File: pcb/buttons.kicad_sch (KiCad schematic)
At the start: 9 parts, among them SW2 SW_DPDT_x2, SW3 SW_DPDT_x2, SW4 RotaryEncoder, SW5 SW_DPDT_x2, SW6 SW_DPDT_x2

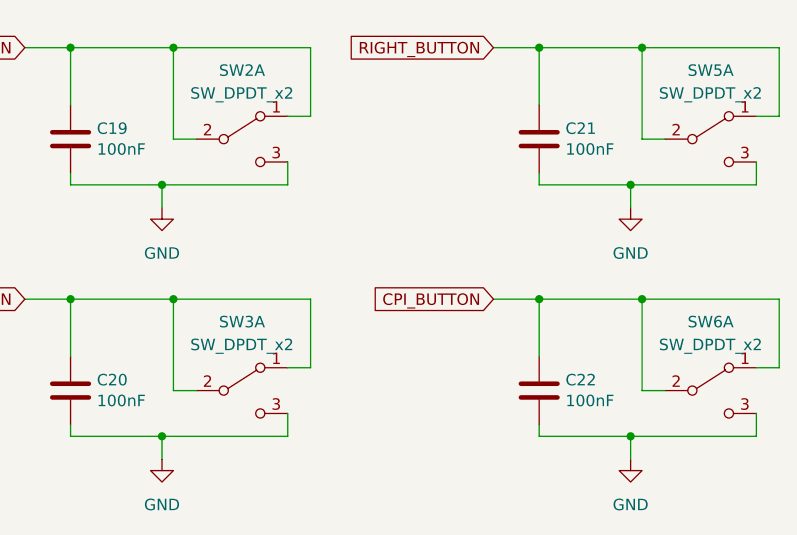
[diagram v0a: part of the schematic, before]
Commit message: cleaned up symbols in schematics a bit
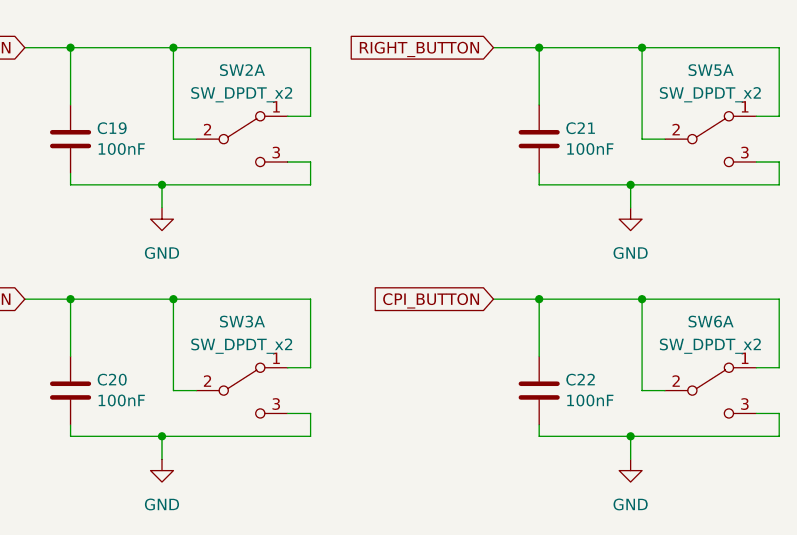
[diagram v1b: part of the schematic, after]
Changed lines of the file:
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@@
     (stroke (width 0) (type default) (color 0 0 0 0))
   )
-  (wire (pts (xy 124.46 96.52) (xy 124.46 93.98))
+  (wire (pts (xy 127 96.52) (xy 127 93.98))
     (stroke (width 0) (type default) (color 0 0 0 0))
   )
@@
     (stroke (width 0) (type default) (color 0 0 0 0))
   )
-  (wire (pts (xy 124.46 124.46) (xy 124.46 121.92))
+  (wire (pts (xy 127 124.46) (xy 127 121.92))
     (stroke (width 0) (type default) (color 0 0 0 0))
   )
   (wire (pts (xy 127 109.22) (xy 127 116.84))
+    (stroke (width 0) (type default) (color 0 0 0 0))
+  )
+  (wire (pts (xy 127 93.98) (xy 124.46 93.98))
     (stroke (width 0) (type default) (color 0 0 0 0))
   )
@@
     (stroke (width 0) (type default) (color 0 0 0 0))
   )
+  (wire (pts (xy 127 121.92) (xy 124.46 121.92))
+    (stroke (width 0) (type default) (color 0 0 0 0))
+  )
   (wire (pts (xy 166.37 119.38) (xy 163.83 119.38))
     (stroke (width 0) (type default) (color 0 0 0 0))
@@
     (stroke (width 0) (type default) (color 0 0 0 0))
   )
-  (wire (pts (xy 176.53 124.46) (xy 176.53 121.92))
+  (wire (pts (xy 179.07 124.46) (xy 179.07 121.92))
     (stroke (width 0) (type default) (color 0 0 0 0))
   )
@@
     (stroke (width 0) (type default) (color 0 0 0 0))
   )
-  (wire (pts (xy 110.49 124.46) (xy 124.46 124.46))
+  (wire (pts (xy 110.49 124.46) (xy 127 124.46))
     (stroke (width 0) (type default) (color 0 0 0 0))
   )
-  (wire (pts (xy 162.56 124.46) (xy 176.53 124.46))
+  (wire (pts (xy 162.56 124.46) (xy 179.07 124.46))
     (stroke (width 0) (type default) (color 0 0 0 0))
   )
-  (wire (pts (xy 110.49 96.52) (xy 124.46 96.52))
+  (wire (pts (xy 110.49 96.52) (xy 127 96.52))
     (stroke (width 0) (type default) (color 0 0 0 0))
   )
@@
   )
   (wire (pts (xy 111.76 109.22) (xy 100.33 109.22))
+    (stroke (width 0) (type default) (color 0 0 0 0))
+  )
+  (wire (pts (xy 179.07 93.98) (xy 176.53 93.98))
     (stroke (width 0) (type default) (color 0 0 0 0))
   )
@@
     (stroke (width 0) (type default) (color 0 0 0 0))
   )
+  (wire (pts (xy 179.07 121.92) (xy 176.53 121.92))
+    (stroke (width 0) (type default) (color 0 0 0 0))
+  )
   (wire (pts (xy 152.4 123.19) (xy 152.4 124.46))
     (stroke (width 0) (type default) (color 0 0 0 0))
@@
     (stroke (width 0) (type default) (color 0 0 0 0))
   )
-  (wire (pts (xy 176.53 96.52) (xy 176.53 93.98))
+  (wire (pts (xy 179.07 96.52) (xy 179.07 93.98))
     (stroke (width 0) (type default) (color 0 0 0 0))
   )
@@
     (stroke (width 0) (type default) (color 0 0 0 0))
   )
-  (wire (pts (xy 162.56 96.52) (xy 176.53 96.52))
+  (wire (pts (xy 162.56 96.52) (xy 179.07 96.52))
     (stroke (width 0) (type default) (color 0 0 0 0))
   )

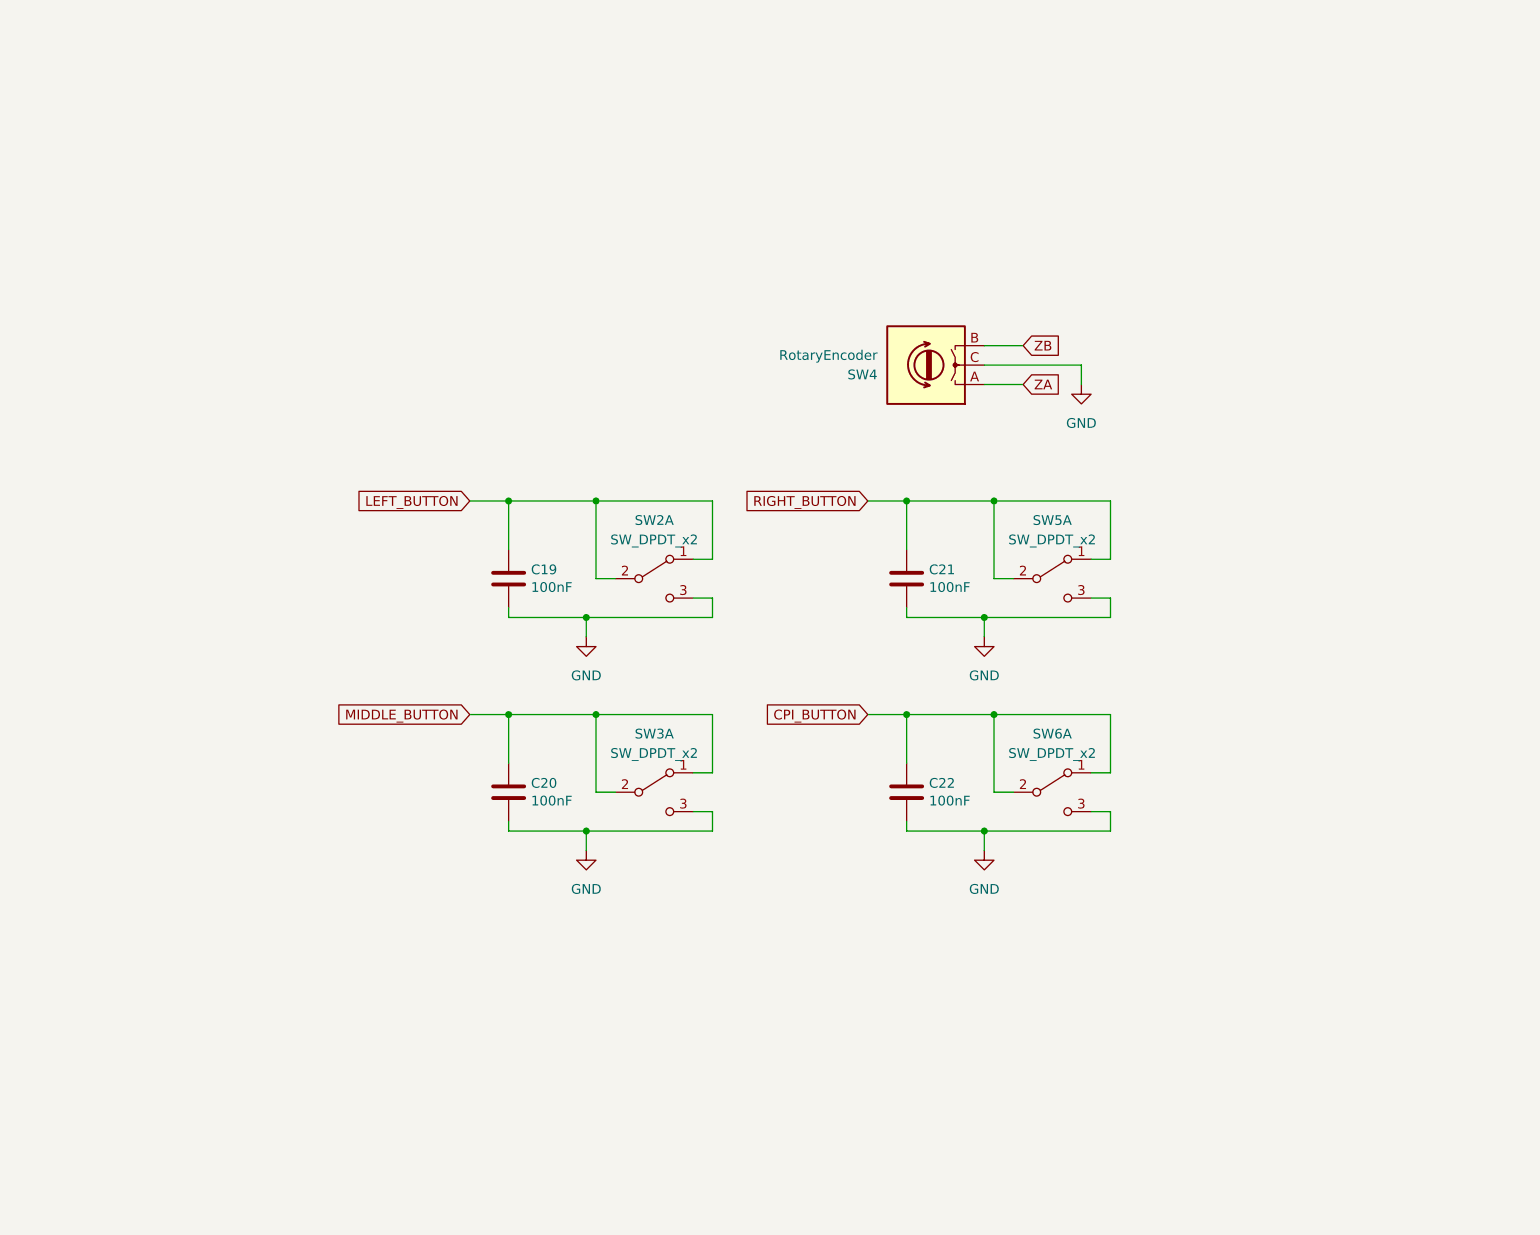
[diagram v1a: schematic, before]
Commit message: - split schematic to lists - changed global ports to local - assigned footprints to majority of schematic parts
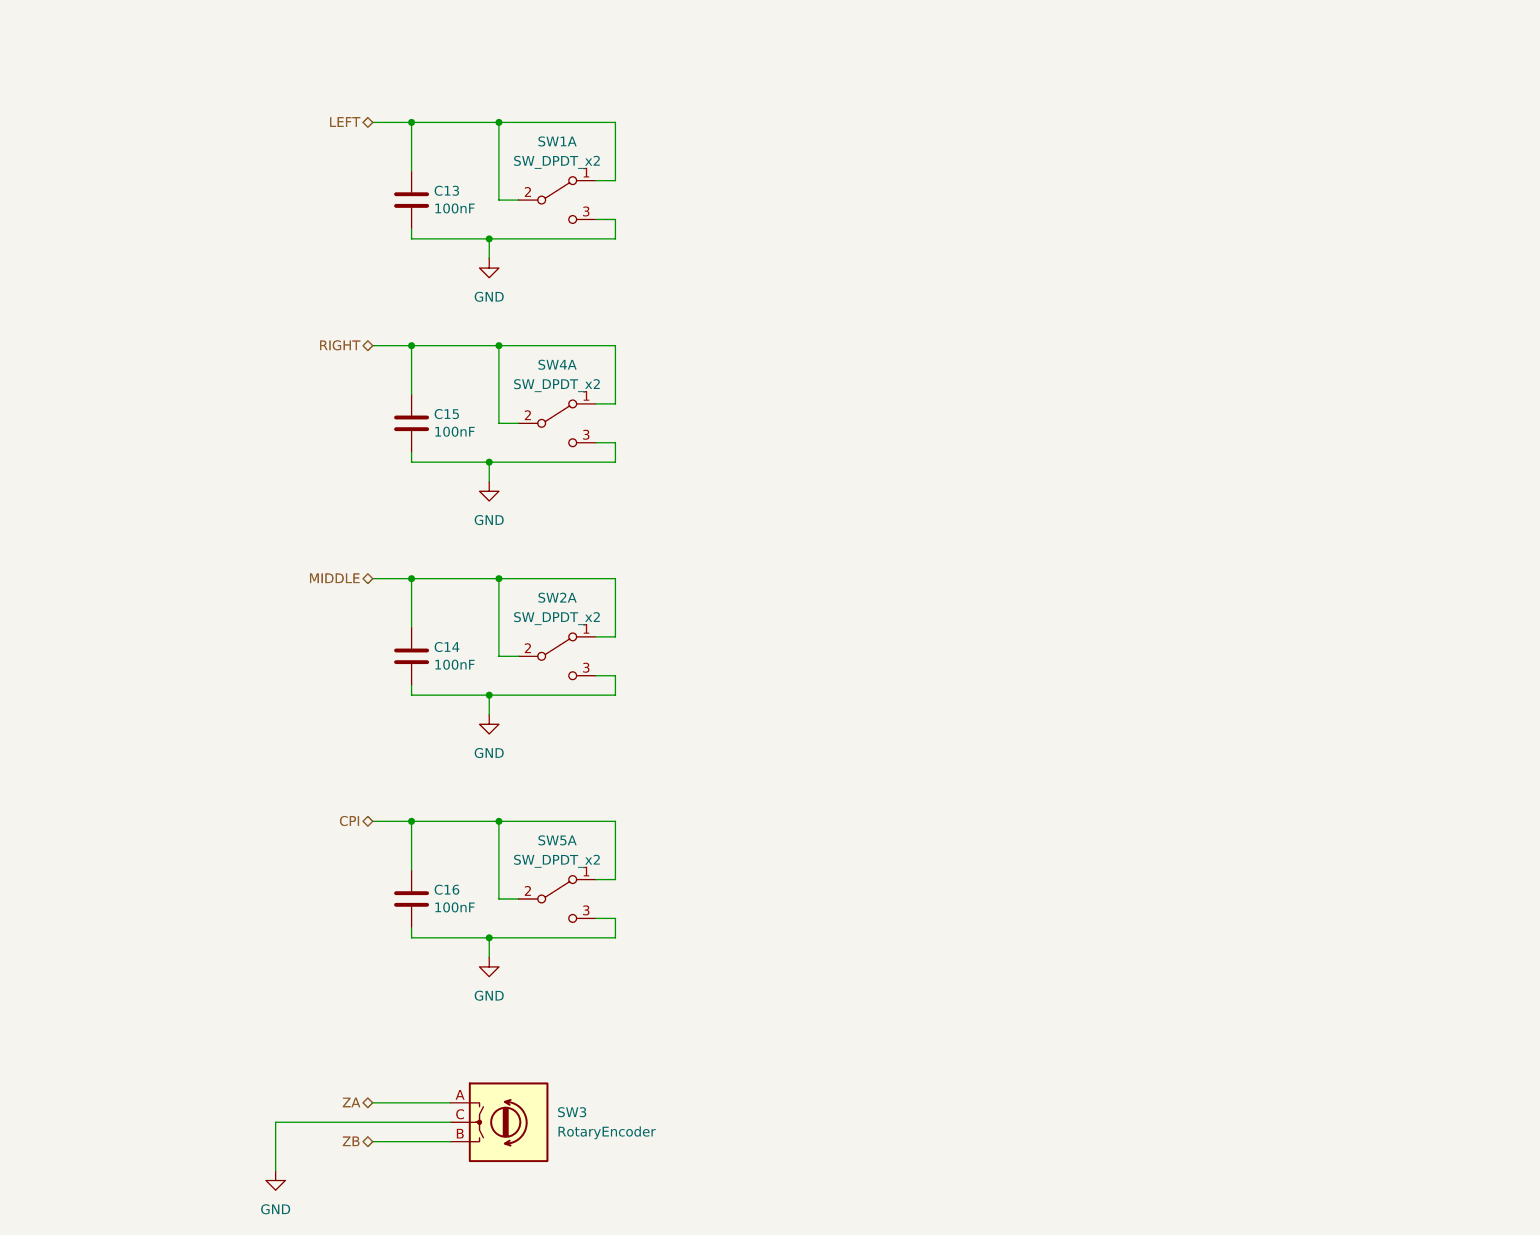
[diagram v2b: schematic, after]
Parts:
- C13: renamed from C19; footprint (none) -> Capacitor_SMD:C_0603_1608Metric
- C14: renamed from C20; footprint (none) -> Capacitor_SMD:C_0603_1608Metric
- C15: renamed from C21; footprint (none) -> Capacitor_SMD:C_0603_1608Metric
- C16: renamed from C22; footprint (none) -> Capacitor_SMD:C_0603_1608Metric
- renumbered SW2 to SW1, SW3 to SW2, SW4 to SW3, SW5 to SW4, SW6 to SW5
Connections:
- net CPI_BUTTON renamed CPI
- net LEFT_BUTTON renamed LEFT
- net MIDDLE_BUTTON renamed MIDDLE
- net RIGHT_BUTTON renamed RIGHT
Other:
- moved on the sheet: C13, C14, C15, C16, SW1A, SW2A, SW3, SW4A, SW5A

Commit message: - added debouncing to buttons - assigned some footprints - added expansion and inspection pin headers
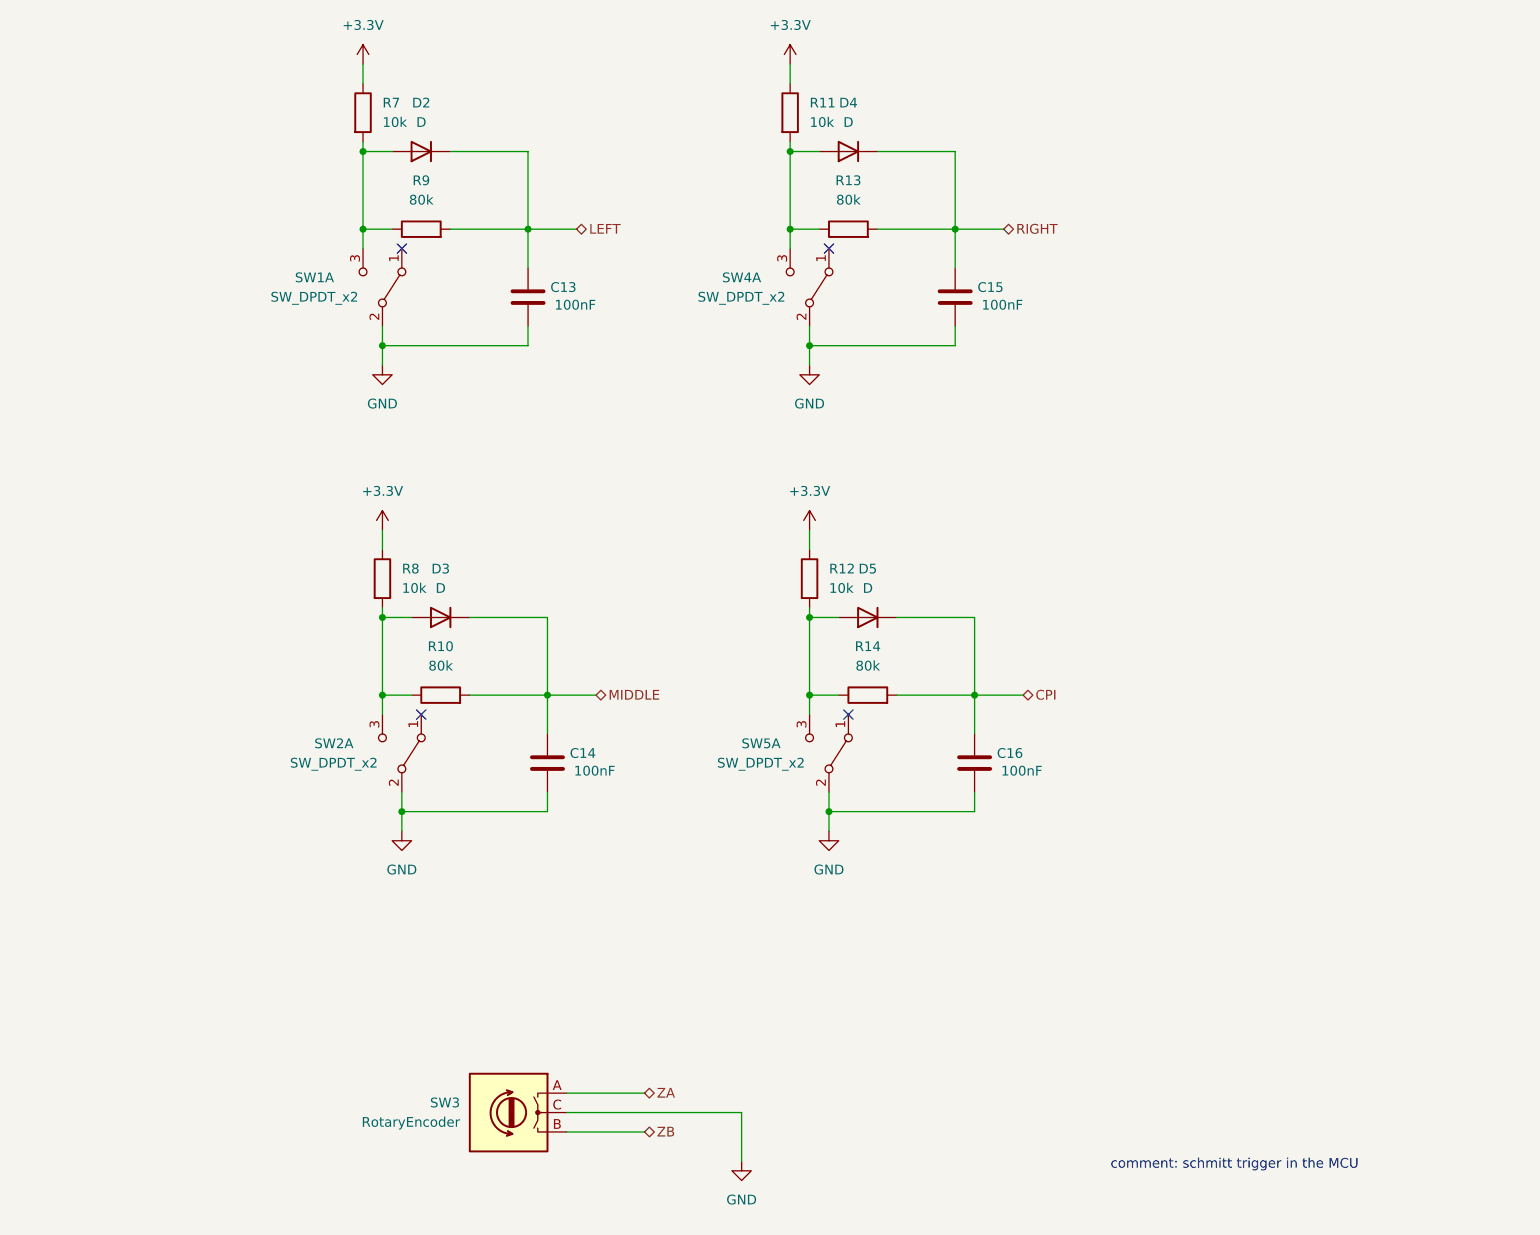
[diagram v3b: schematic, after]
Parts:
- added D2, D3, D4, D5: D, Diode_SMD:D_0603_1608Metric, symbol Device:D
- added R10, R13, R14, R9: 80k, Resistor_SMD:R_0603_1608Metric, symbol Device:R
- added R11, R12, R7, R8: 10k, Resistor_SMD:R_0603_1608Metric, symbol Device:R
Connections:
- net CPI: now also D5.1 (K), R14.2; no longer SW5.1 (A), SW5.2 (B)
- net GND: now also SW1.2 (B), SW2.2 (B), SW4.2 (B), SW5.2 (B); no longer SW1.3 (C), SW2.3 (C), SW4.3 (C), SW5.3 (C)
- net LEFT: now also D2.1 (K), R9.2; no longer SW1.1 (A), SW1.2 (B)
- net MIDDLE: now also D3.1 (K), R10.2; no longer SW2.1 (A), SW2.2 (B)
- net RIGHT: now also D4.1 (K), R13.2; no longer SW4.1 (A), SW4.2 (B)
- new net: D3.2 (A), R10.1, R8.2, SW2.3 (C)
- new net: D2.2 (A), R7.2, R9.1, SW1.3 (C)
- new net: D5.2 (A), R12.2, R14.1, SW5.3 (C)
- new net: D4.2 (A), R11.2, R13.1, SW4.3 (C)
- new net +3V3: R11.1, R12.1, R7.1, R8.1
- no-connect marks 0 -> 4
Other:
- note added: "comment: schmitt trigger in the MCU"
- moved on the sheet: C13, SW1A, SW3
